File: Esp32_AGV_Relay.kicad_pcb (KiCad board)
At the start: 2 copper layers, 45.6 x 38.1 mm, 19 parts, among them J1 Sensor, J2 LCD1602, J3 Barcode Reader, J4 Left, J5 Conn_01x06, J6 Conn_01x06, J7 Reset, J8 right, Q1 BSS138, Q2 BSS138, U1 PC817

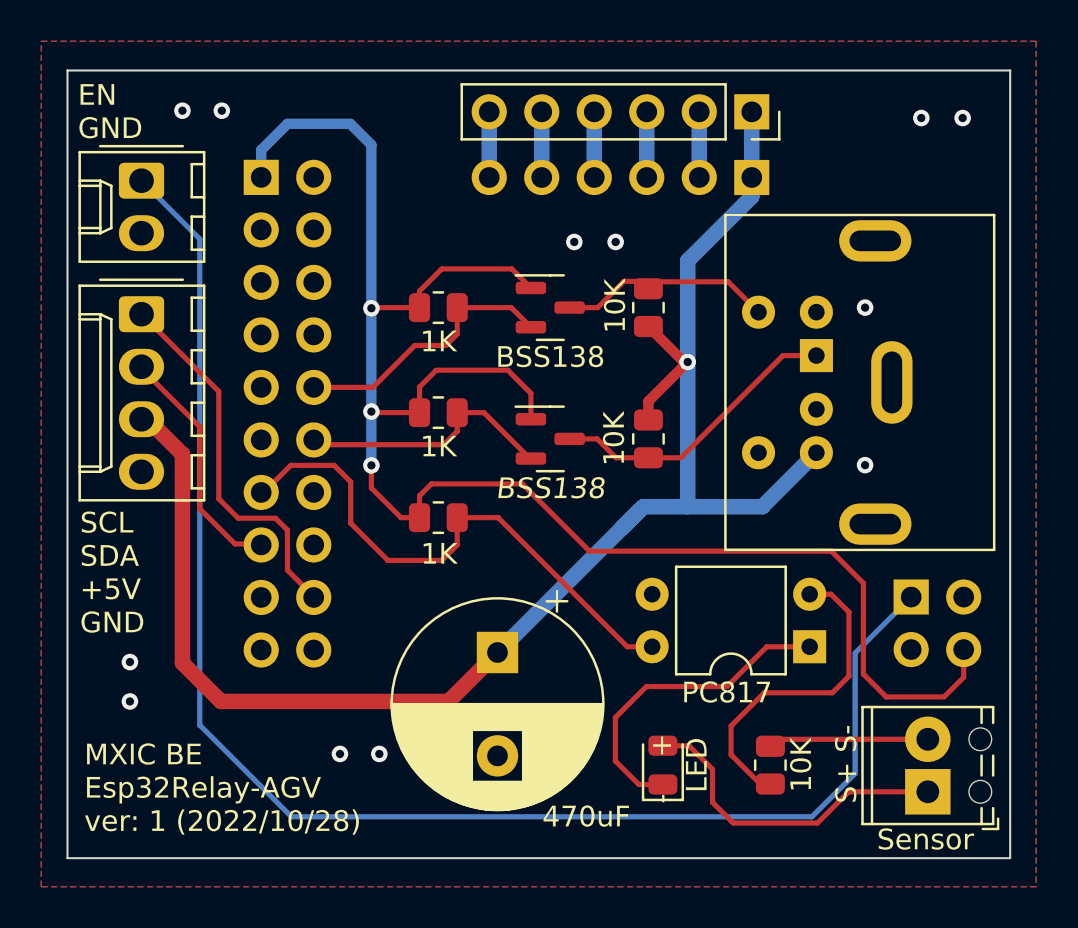
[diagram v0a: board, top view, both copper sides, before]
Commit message: v2
1. 改成下拉電阻
2. 更換連接器
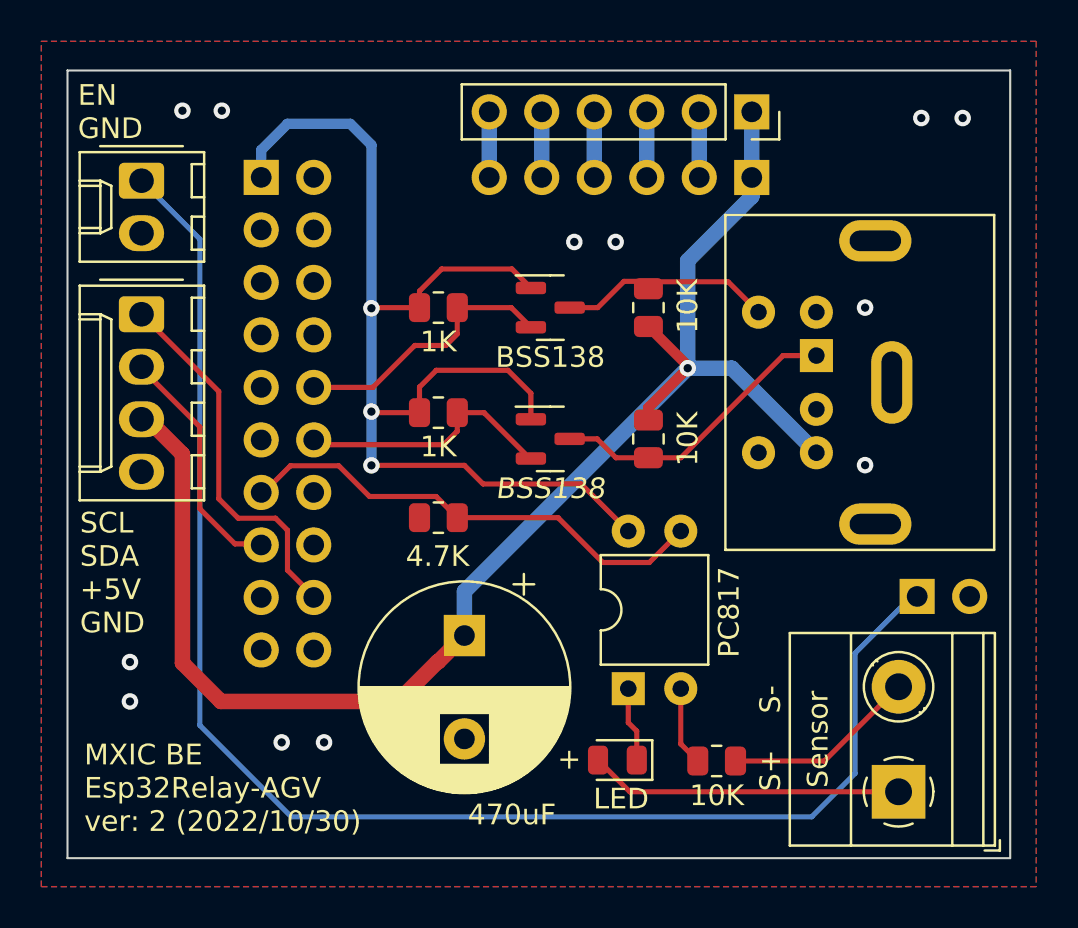
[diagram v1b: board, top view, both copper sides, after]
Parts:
- removed the R2 at (136.8, 113.0)
- added R5: 4.7K, Resistor_SMD:R_0805_2012Metric, F.Cu at (136.8, 113.0)
- J6: renamed from J1; footprint TerminalBlock_Phoenix:TerminalBlock_Phoenix_MPT-0,5-2-2.54_1x02_P2.54mm_Horizontal -> TerminalBlock_Phoenix:TerminalBlock_Phoenix_MKDS-1,5-2-5.08_1x02_P5.08mm_Horizontal
- J8: footprint Connector_PinSocket_2.54mm:PinSocket_2x02_P2.54mm_Vertical -> Connector_PinSocket_2.54mm:PinSocket_1x02_P2.54mm_Vertical
- moved U1 9.01 mm to (146.0, 121.3), turned to 90 degrees
- moved R3 2.61 mm to (150.3, 124.8), turned to 0 degrees
- moved D1 2.21 mm to (145.5, 124.8), turned to 180 degrees
- moved C1 1.80 mm to (138.1, 118.7)
- moved J6 1.41 mm to (159.1, 126.3)
- moved J8 0.29 mm to (160.0, 116.8), turned to -90 degrees
- renumbered J2 to J1, J5 to J2, J6 to J3, J3 to J4, J4 to J5, R3 to R1, R4 to R2, R1 to R3, R5 to R4
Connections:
- J4 pad 7: GND -> (no net)
- J8 pad 2: GND -> unconnected-(J8-Pad2)
- U1 pad 3: GND -> IO19
- U1 pad 4: IO19 -> +3.3V
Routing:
- net +3.3V: track 83.2 -> 56.8 mm
- net Net-(R3-Pad1): track 15.9 -> 3.84 mm
- net Net-(D1-Pad1): track 15.7 -> 3.63 mm
- net +5V: track 77.1 -> 73.6 mm
- net IO19: track 26.7 -> 23.4 mm
- net Net-(J6-Pad2): track 7.75 -> 9.37 mm
- net Net-(D1-Pad2): track 15.9 -> 15.2 mm
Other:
- board text added: "+"
- board text added: "MXIC BE Esp32Relay-AGV ver: 2 (2022/10/30)"
- board text removed: "- +"
- board text removed: "MXIC BE Esp32Relay-AGV ver: 1 (2022/10/28)"
